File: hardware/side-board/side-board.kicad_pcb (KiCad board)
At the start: 4 copper layers, 87.5 x 50.6 mm, 298 parts, among them IC101 TPS62933DRLR, IC102 NUP2105LT1G, IC201 STM32C092KCT6, IC202 TCAN332DR, IC203 TPS56A37RPAR, IC204 INA181A1IDBVR, IC301 STM32C092KCT6, IC302 TCAN332DR, IC303 TPS56A37RPAR, IC304 INA181A1IDBVR, IC401 STM32C092KCT6, IC402 TCAN332DR, IC403 TPS56A37RPAR, IC404 INA181A1IDBVR, J101 Inter-board Connector, J102 Inter-board Connector, J103 XT30 VBAT, J104 SWD PWR, J201 Servo Connector, J202 Servo Connector, J203 Servo Connector, J205 ToF, J301 Servo Connector, J302 Servo Connector, J303 Servo Connector, J305 ToF, J401 Servo Connector, J402 Servo Connector, J403 Servo Connector, J405 ToF, Y201 Crystal_GND24, Y301 Crystal_GND24, Y401 Crystal_GND24

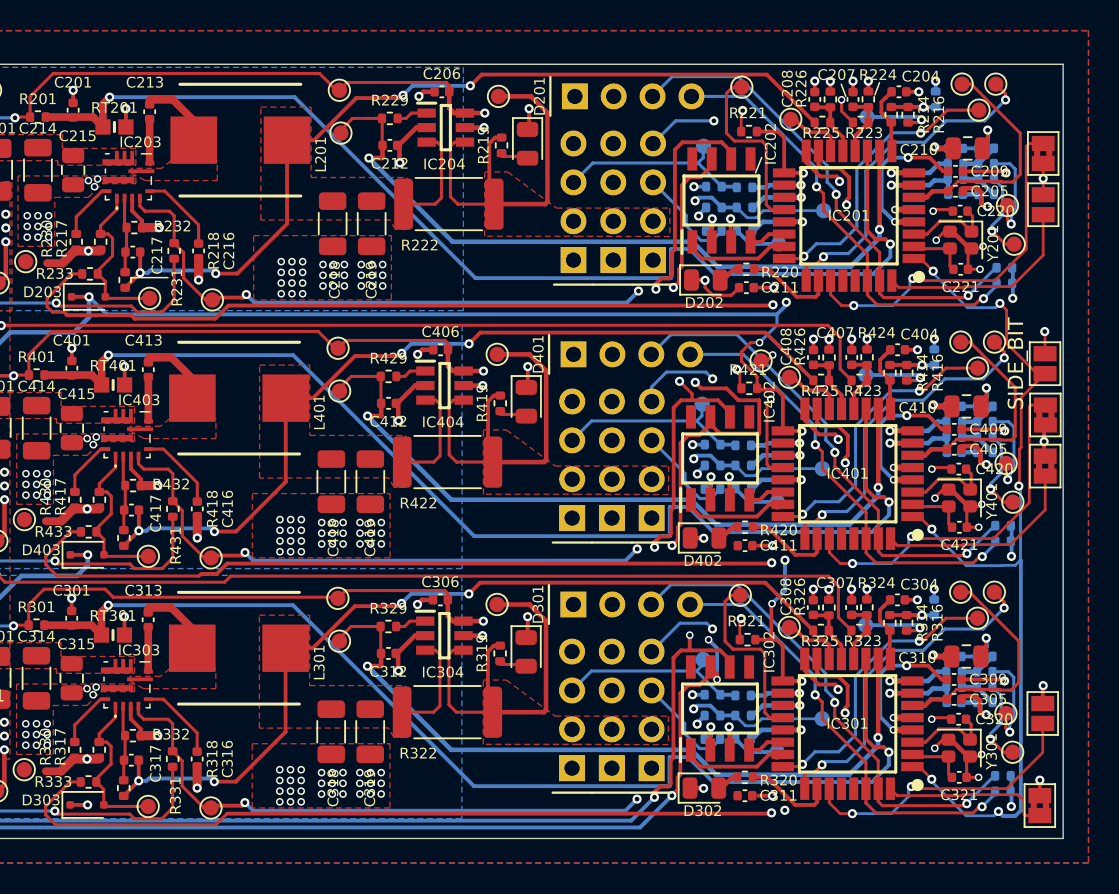
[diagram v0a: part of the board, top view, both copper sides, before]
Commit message: Fixed DRC errors
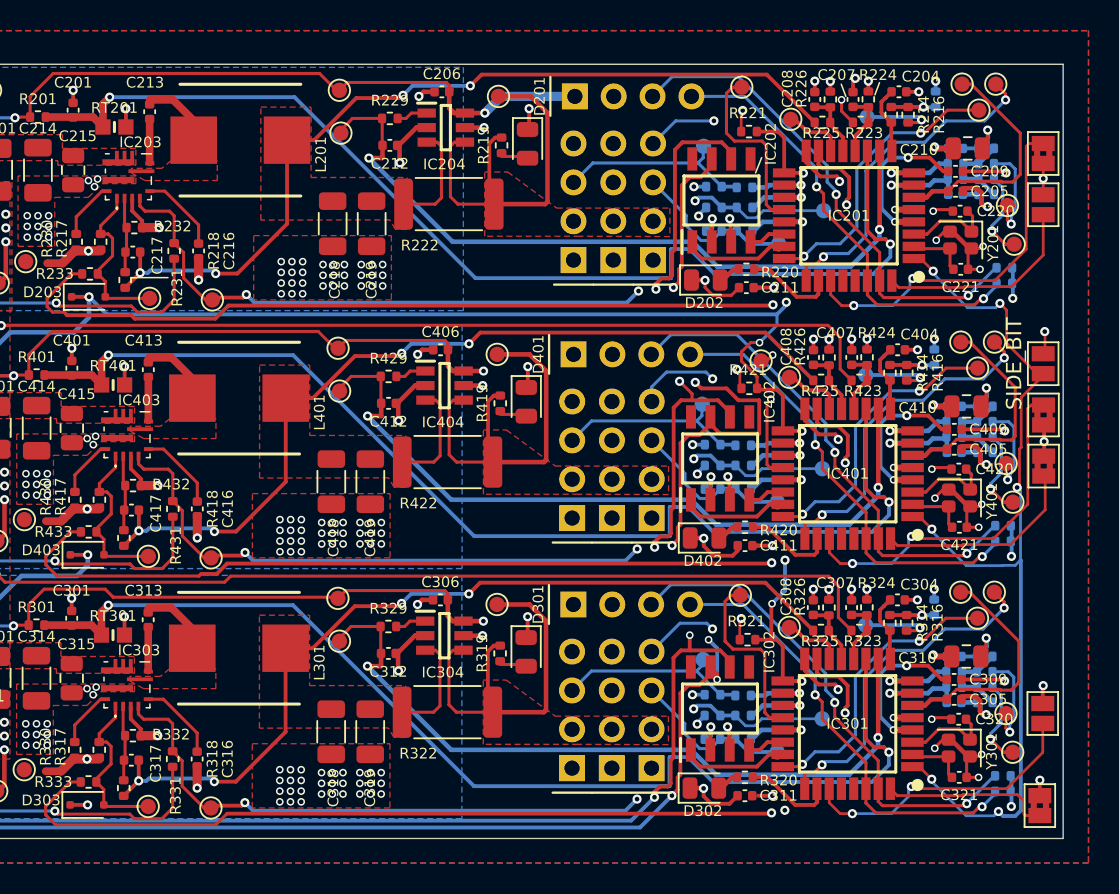
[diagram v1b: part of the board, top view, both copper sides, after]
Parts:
- moved JP106 0.12 mm to (226.4, 59.5)
- moved JP107 0.12 mm to (226.4, 56.2)
- moved JP105 0.10 mm to (226.4, 62.9)
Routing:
- net +3V3: track 290.7 -> 325.6 mm
- net GND: track 130.9 -> 137.7 mm
- net /Leg_C/MCU_BUCK_EN: track 60.0 -> 66.5 mm
- net /Leg_B/MCU_BUCK_EN: track 59.9 -> 66.5 mm
- net /Leg_C/PWM_TIBIA: track 9.80 -> 10.8 mm
- net /Leg_A/PWM_TIBIA: track 9.80 -> 10.8 mm
- net /Leg_B/PWM_TIBIA: track 9.80 -> 10.8 mm

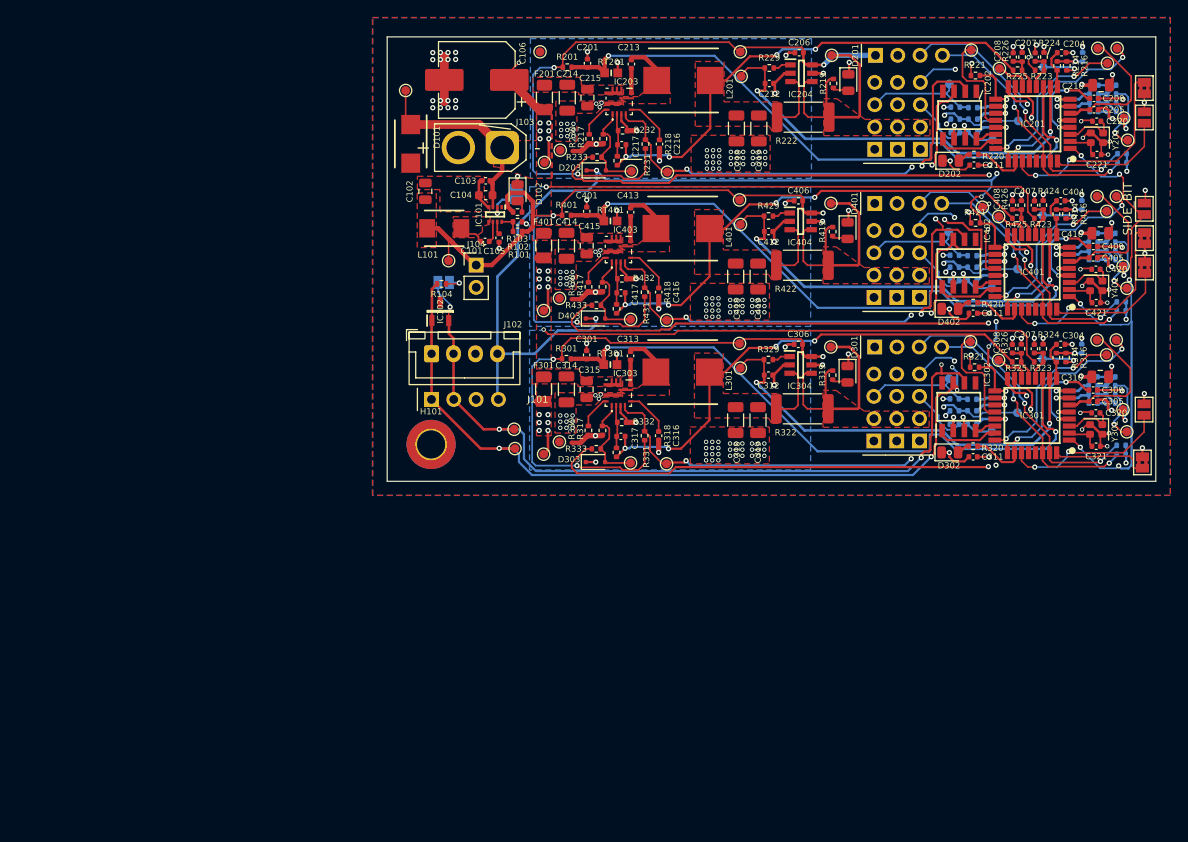
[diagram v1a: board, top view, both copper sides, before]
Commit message: Updated B Silkscreen layer
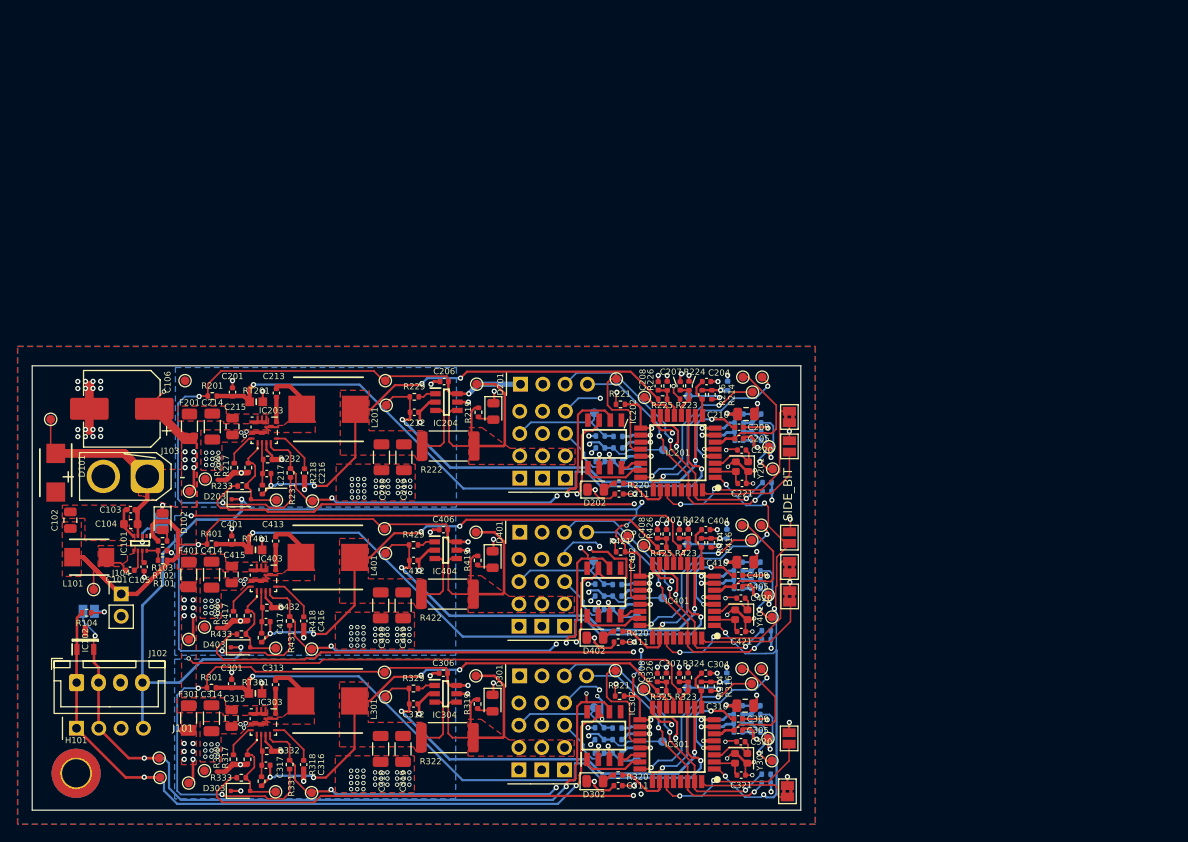
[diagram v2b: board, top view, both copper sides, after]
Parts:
- moved C101 55.1 mm to (110.9, 97.3)
- moved C104 55.1 mm to (111.0, 92.1)
- moved C106 55.1 mm to (110.0, 78.9)
- moved C204 55.1 mm to (176.6, 75.8)
- moved C207 55.1 mm to (173.6, 76.3)
- moved C208 55.1 mm to (171.1, 76.3)
- moved C210 55.1 mm to (181.1, 79.5)
- moved C211 55.1 mm to (166.6, 88.6)
- moved C217 55.1 mm to (126.5, 86.3)
- moved C218 55.1 mm to (139.5, 84.5)
- moved C220 55.1 mm to (180.6, 83.6)
- moved C301 55.1 mm to (122.5, 110.2)
- moved C302 55.1 mm to (180.2, 115.7)
- moved C303 55.1 mm to (180.2, 112.7)
- moved C304 55.1 mm to (176.5, 109.0)
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
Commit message: Added logo to sideboard
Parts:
- added G***: LOGO, LOGO, B.Cu at (106.3, 95.5)
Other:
- board text added: "SIDE BOARD"
- board text added: "VECTOR"
